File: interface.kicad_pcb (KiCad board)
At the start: 2 copper layers, 36.8 x 66 mm, 35 parts, among them U1 THERMAL, U2 SX1308

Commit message: finish pcb
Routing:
- added copper zone on B.Cu, net GND
- added copper zone on F.Cu, net GND
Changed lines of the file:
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@@
   (segment (start 141.6 80.6) (end 141.6 75) (width 0.25) (layer F.Cu) (net 52))
   (segment (start 139.4 82.8) (end 141.6 80.6) (width 0.25) (layer F.Cu) (net 52))
+  (zone (net 2) (net_name GND) (layer F.Cu) (hatch edge 0.508)
+    (connect_pads (clearance 0.508))
+    (min_thickness 0.254)
+    (fill yes (arc_segments 16) (thermal_gap 0.508) (thermal_bridge_width 0.508))
+    (polygon
+      (pts
+        (xy 161.3 120.7) (xy 124.5 120.6) (xy 124.5 54.6) (xy 161.3 54.6)
+      )
+    )
+  )
+  (zone (net 2) (net_name GND) (layer B.Cu) (hatch edge 0.508)
+    (connect_pads (clearance 0.508))
+    (min_thickness 0.254)
+    (fill yes (arc_segments 16) (thermal_gap 0.508) (thermal_bridge_width 0.508))
+    (polygon
+      (pts
+        (xy 161.3 120.6) (xy 124.5 120.6) (xy 124.5 54.6) (xy 161.3 54.6)
+      )
+    )
+  )
 )

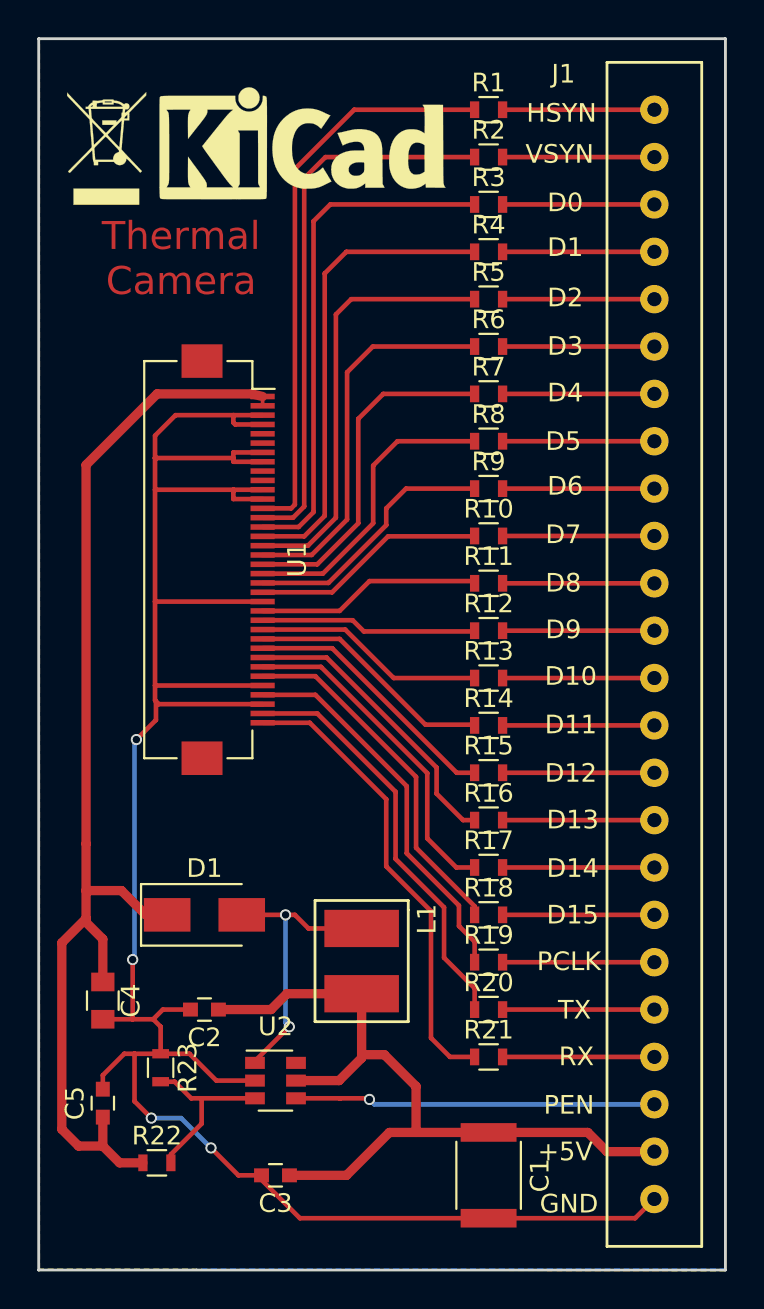
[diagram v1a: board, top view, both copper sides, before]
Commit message: Revert "finish pcb"
This reverts commit 664f2069ac5b8cd3e927f5ba02bd3a98c86c313e.
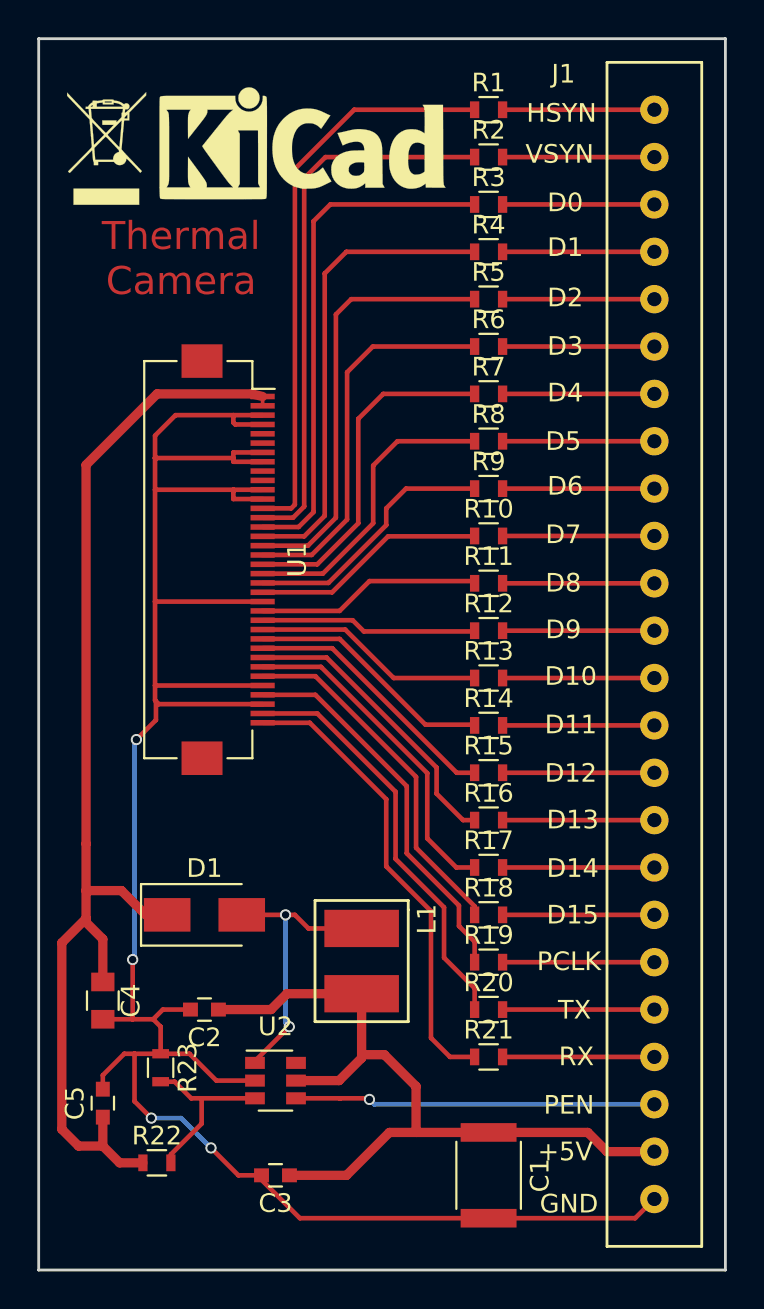
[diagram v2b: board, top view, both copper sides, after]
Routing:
- removed copper zone on B.Cu, net GND
- removed copper zone on F.Cu, net GND
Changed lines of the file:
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@@
   (segment (start 141.6 80.6) (end 141.6 75) (width 0.25) (layer F.Cu) (net 52))
   (segment (start 139.4 82.8) (end 141.6 80.6) (width 0.25) (layer F.Cu) (net 52))
-  (zone (net 2) (net_name GND) (layer F.Cu) (hatch edge 0.508)
-    (connect_pads (clearance 0.508))
-    (min_thickness 0.254)
-    (fill yes (arc_segments 16) (thermal_gap 0.508) (thermal_bridge_width 0.508))
-    (polygon
-      (pts
-        (xy 161.3 120.7) (xy 124.5 120.6) (xy 124.5 54.6) (xy 161.3 54.6)
-      )
-    )
-  )
-  (zone (net 2) (net_name GND) (layer B.Cu) (hatch edge 0.508)
-    (connect_pads (clearance 0.508))
-    (min_thickness 0.254)
-    (fill yes (arc_segments 16) (thermal_gap 0.508) (thermal_bridge_width 0.508))
-    (polygon
-      (pts
-        (xy 161.3 120.6) (xy 124.5 120.6) (xy 124.5 54.6) (xy 161.3 54.6)
-      )
-    )
-  )
 )
